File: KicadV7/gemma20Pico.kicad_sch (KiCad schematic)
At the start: 13 parts, among them J1-Prox1 I2C_CH0, J2-Prox0 I2C_CH1, J3-Motor1 DC-Motor, J4-BAT1 3.7V Battery, J5-Servo1 Servo, J6-Pot1 Pot, J7-Pot2 Pot, M1 Motor_DC, M2 Motor_Servo, U1-RPI-Pico1 Pico

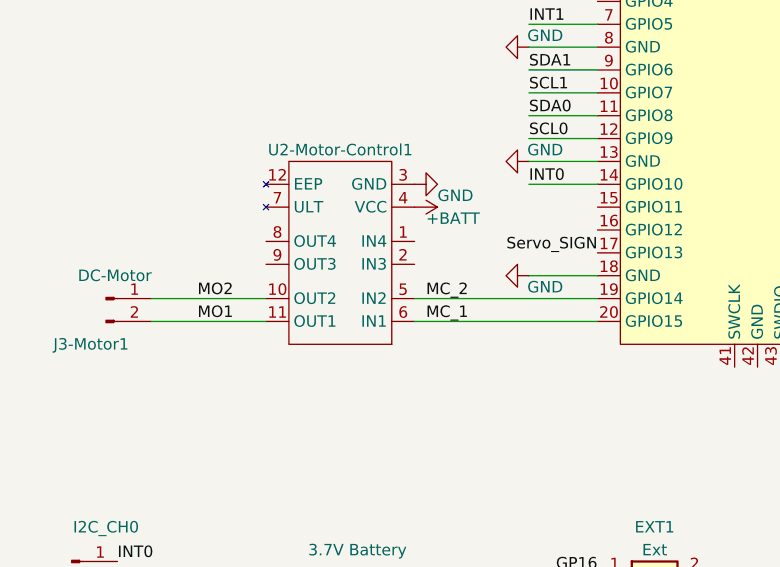
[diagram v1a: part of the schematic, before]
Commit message: Connect H bridges in paralell
Connect H-Bridges in paralell for 2xcurrent, added mounting holes , reduced board size to allow G9 Servo mount moved  and rotated  POT  for easyer access to +3.3V
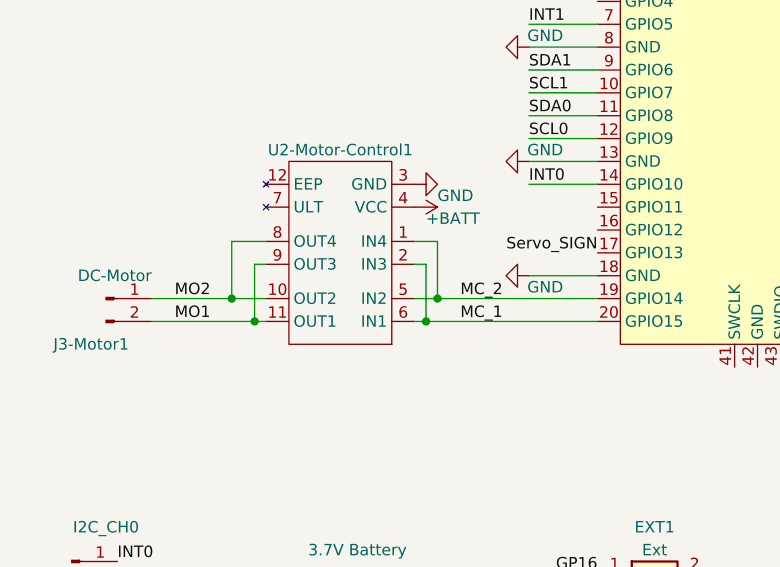
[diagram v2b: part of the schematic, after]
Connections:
- net MC_1: now also U2-Motor-Control1.2 (IN3)
- net MC_2: now also U2-Motor-Control1.1 (IN4)
- net MO1: now also U2-Motor-Control1.9 (OUT3)
- net MO2: now also U2-Motor-Control1.8 (OUT4)
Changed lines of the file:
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@@
   (junction (at 106.68 124.46) (diameter 0) (color 0 0 0 0)
   )
+  (junction (at 74.93 91.44) (diameter 0) (color 0 0 0 0)
+  )
+  (junction (at 53.34 88.9) (diameter 0) (color 0 0 0 0)
+  )
   (junction (at 106.68 121.92) (diameter 0) (color 0 0 0 0)
   )
+  (junction (at 55.88 91.44) (diameter 0) (color 0 0 0 0)
+  )
+  (junction (at 76.2 88.9) (diameter 0) (color 0 0 0 0)
+  )
   (junction (at 106.68 125.73) (diameter 0) (color 0 0 0 0)
   )
@@
   (junction (at 106.68 129.54) (diameter 0) (color 0 0 0 0)
   )
-  (wire (pts (xy 73.66 88.9) (xy 93.98 88.9))
+  (wire (pts (xy 73.66 88.9) (xy 76.2 88.9))
     (stroke (width 0) (type default))
   )
@@
     (stroke (width 0) (type default))
   )
-  (wire (pts (xy 73.66 91.44) (xy 93.98 91.44))
+  (wire (pts (xy 53.34 82.55) (xy 53.34 88.9))
+    (stroke (width 0) (type default))
+  )
+  (wire (pts (xy 73.66 91.44) (xy 74.93 91.44))
     (stroke (width 0) (type default))
   )
@@
     (stroke (width 0) (type default))
   )
+  (wire (pts (xy 73.66 82.55) (xy 76.2 82.55))
+    (stroke (width 0) (type default))
+  )
   (wire (pts (xy 129.54 73.66) (xy 135.89 73.66))
     (stroke (width 0) (type default))
@@
     (stroke (width 0) (type default))
   )
-  (wire (pts (xy 57.15 88.9) (xy 44.45 88.9))
+  (wire (pts (xy 57.15 88.9) (xy 53.34 88.9))
+    (stroke (width 0) (type default))
+  )
+  (wire (pts (xy 76.2 82.55) (xy 76.2 88.9))
+    (stroke (width 0) (type default))
+  )
+  (wire (pts (xy 55.88 85.09) (xy 55.88 91.44))
     (stroke (width 0) (type default))
   )
@@
     (stroke (width 0) (type default))
   )
+  (wire (pts (xy 74.93 91.44) (xy 93.98 91.44))
+    (stroke (width 0) (type default))
+  )
   (wire (pts (xy 106.68 119.38) (xy 106.68 121.92))
     (stroke (width 0) (type default))
   )
+  (wire (pts (xy 44.45 91.44) (xy 55.88 91.44))
+    (stroke (width 0) (type default))
+  )
+  (wire (pts (xy 76.2 88.9) (xy 93.98 88.9))
+    (stroke (width 0) (type default))
+  )
   (wire (pts (xy 201.93 118.11) (xy 209.55 118.11))
     (stroke (width 0) (type default))
@@
     (stroke (width 0) (type default))
   )
-  (wire (pts (xy 57.15 91.44) (xy 44.45 91.44))
+  (wire (pts (xy 57.15 91.44) (xy 55.88 91.44))
     (stroke (width 0) (type default))
   )
@@
     (stroke (width 0) (type default))
   )
+  (wire (pts (xy 57.15 85.09) (xy 55.88 85.09))
+    (stroke (width 0) (type default))
+  )
+  (wire (pts (xy 74.93 85.09) (xy 74.93 91.44))
+    (stroke (width 0) (type default))
+  )
   (wire (pts (xy 86.36 63.5) (xy 93.98 63.5))
     (stroke (width 0) (type default))
   )
+  (wire (pts (xy 53.34 88.9) (xy 44.45 88.9))
+    (stroke (width 0) (type default))
+  )
+  (wire (pts (xy 73.66 85.09) (xy 74.93 85.09))
+    (stroke (width 0) (type default))
+  )
   (wire (pts (xy 86.36 71.12) (xy 93.98 71.12))
     (stroke (width 0) (type default))
@@
     (stroke (width 0) (type default))
   )
+  (wire (pts (xy 57.15 82.55) (xy 53.34 82.55))
+    (stroke (width 0) (type default))
+  )
   (label "GP17" (at 129.54 88.9 0) (fields_autoplaced)
     (effects (font (size 1.27 1.27)) (justify left bottom))
@@
     (effects (font (size 1.27 1.27)) (justify left bottom))
   )
-  (label "MO1" (at 49.53 91.44 0) (fields_autoplaced)
+  (label "MO1" (at 46.99 91.44 0) (fields_autoplaced)
     (effects (font (size 1.27 1.27)) (justify left bottom))
   )
@@
     (effects (font (size 1.27 1.27)) (justify left bottom))
   )
-  (label "MO2" (at 49.53 88.9 0) (fields_autoplaced)
+  (label "MO2" (at 46.99 88.9 0) (fields_autoplaced)
     (effects (font (size 1.27 1.27)) (justify left bottom))
   )
@@
     (effects (font (size 1.27 1.27)) (justify left bottom))
   )
-  (label "MC_2" (at 74.93 88.9 0) (fields_autoplaced)
+  (label "MC_2" (at 78.74 88.9 0) (fields_autoplaced)
     (effects (font (size 1.27 1.27)) (justify left bottom))
   )
@@
     (effects (font (size 1.27 1.27)) (justify left bottom))
   )
-  (label "MC_1" (at 74.93 91.44 0) (fields_autoplaced)
-    (effects (font (size 1.27 1.27)) (justify left bottom))
-  )
+  (label "MC_1" (at 78.74 91.44 0) (fields_autoplaced)
+    (effects (font (size 1.27 1.27)) (justify left bottom))
+  )

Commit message: Addad title head info
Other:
- company: (none) -> Rune Langøy
- title: (none) -> PicoRC
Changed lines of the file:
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@@
 (kicad_sch (version 20230121) (generator eeschema)
   (paper "A4")
+  (title_block
+    (title "PicoRC")
+    (date "2023-07-12")
+    (rev "1.1")
+    (company "Rune Langøy")
+    (comment 1 "File repo https://github.com/rlangoy/RCPico")
+  )
   (junction (at 106.68 124.46) (diameter 0) (color 0 0 0 0)
   )

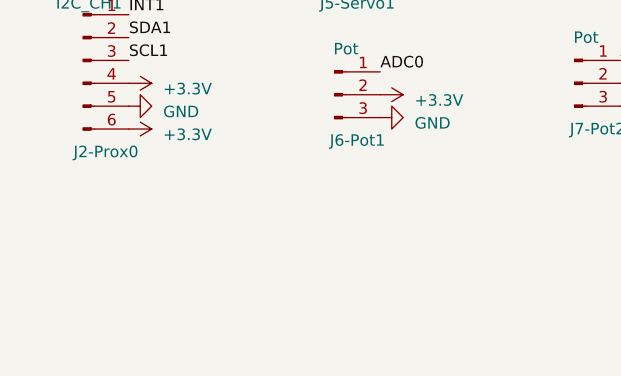
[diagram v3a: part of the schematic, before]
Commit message: Added decoupling capacitor for the Pico amd added description
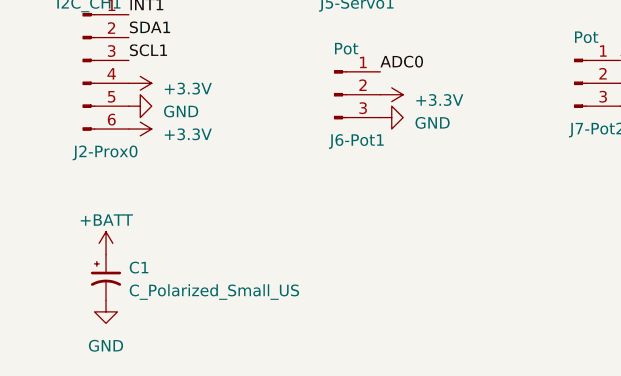
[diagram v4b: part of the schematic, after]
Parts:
- added C1: C_Polarized_Small_US, Capacitor_THT:CP_Radial_D5.0mm_P2.50mm, symbol Device:C_Polarized_Small_US
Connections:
- net +BATT: now also C1.1
- net GND: now also C1.2
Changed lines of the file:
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@@
+    )
+  )
+  (symbol (lib_id "power:GND") (at 39.37 175.26 0) (unit 1)
+    (in_bom yes) (on_board yes) (dnp no) (fields_autoplaced)
+    (property "Reference" "#PWR032" (at 39.37 181.61 0)
+      (effects (font (size 1.27 1.27)) hide)
+    )
+    (property "Value" "GND" (at 39.37 180.34 0)
+      (effects (font (size 1.27 1.27)))
+    )
+    (property "Footprint" "" (at 39.37 175.26 0)
+      (effects (font (size 1.27 1.27)) hide)
+    )
+    (property "Datasheet" "" (at 39.37 175.26 0)
+      (effects (font (size 1.27 1.27)) hide)
+    )
+    (pin "1")
+    (instances
+      (project "gemma20Pico"
+        (path "/b10b7441-68fa-49c0-9dad-fceb534010fc"
+          (reference "#PWR032") (unit 1)
+        )
+      )
+    )
+  )
+  (symbol (lib_id "Device:C_Polarized_Small_US") (at 39.37 172.72 0) (unit 1)
+    (in_bom yes) (on_board yes) (dnp no) (fields_autoplaced)
+    (property "Reference" "C1" (at 41.91 171.6532 0)
+      (effects (font (size 1.27 1.27)) (justify left))
+    )
+    (property "Value" "C_Polarized_Small_US" (at 41.91 174.1932 0)
+      (effects (font (size 1.27 1.27)) (justify left))
+    )
+    (property "Footprint" "Capacitor_THT:CP_Radial_D5.0mm_P2.50mm" (at 39.37 172.72 0)
+      (effects (font (size 1.27 1.27)) hide)
+    )
+    (property "Datasheet" "~" (at 39.37 172.72 0)
+      (effects (font (size 1.27 1.27)) hide)
+    )
+    (pin "1")
+    (pin "2")
+    (instances
+      (project "gemma20Pico"
+        (path "/b10b7441-68fa-49c0-9dad-fceb534010fc"
+          (reference "C1") (unit 1)
+        )
+      )
     )
   )
@@
         )
       )
+    )
+  )
+  (symbol (lib_id "power:+BATT") (at 39.37 170.18 0) (unit 1)
+    (in_bom yes) (on_board yes) (dnp no) (fields_autoplaced)
+    (property "Reference" "#PWR029" (at 39.37 173.99 0)
+      (effects (font (size 1.27 1.27)) hide)
+    )
+    (property "Value" "+BATT" (at 39.37 166.37 0)
+      (effects (font (size 1.27 1.27)))
+    )
+    (property "Footprint" "" (at 39.37 170.18 0)
+      (effects (font (size 1.27 1.27)) hide)
+    )
+    (property "Datasheet" "" (at 39.37 170.18 0)
+      (effects (font (size 1.27 1.27)) hide)
+    )
+    (pin "1")
+    (instances
+      (project "gemma20Pico"
+        (path "/b10b7441-68fa-49c0-9dad-fceb534010fc"
+          (reference "#PWR029") (unit 1)
+        )
+      )
